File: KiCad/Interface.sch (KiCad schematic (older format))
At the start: 22 parts, among them J301 IR LED, J302 Button, SW301 Reset, SW302 Push 1, SW303 Push 2, U301 ULN2003

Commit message: Schematic Version 4 Some Software Changes
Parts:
- removed D301: LRTBG6TG, ledbox-newfootprints:LED-6-BIG, symbol LRTBG6TG
- removed R304: 150, Resistors_SMD:R_0805, symbol R
- removed R305, R311: 82, Resistors_SMD:R_0805, symbol R
- removed R306, R307: 22, Resistors_SMD:R_0805, symbol R
- removed U301: ULN2003, Housings_SOIC:SOIC-16_3.9x9.9mm_Pitch1.27mm, symbol ULN2003
- added C? (x2): 10u, Capacitors_SMD:C_0805, symbol C
- added JP?: IR 24mA, SMD_Jumper:Jumper_SMD_02, symbol Jumper_NO_Small
- added JP?: IR 48mA, SMD_Jumper:Jumper_SMD_02, symbol Jumper_NO_Small
- added JP?: IR 12mA, SMD_Jumper:Jumper_SMD_02, symbol Jumper_NO_Small
- added Q?: NTR4003N, TO_SOT_Packages_SMD:SOT-23, symbol Q_NMOS_GSD
- added R?: 100, Resistors_SMD:R_0805, symbol R
- added R?: 300, Resistors_SMD:R_0805, symbol R
- added R?: 150, Resistors_SMD:R_0805, symbol R
- added R?: 75, Resistors_SMD:R_0805, symbol R
- added R?: 100k, Resistors_SMD:R_0805, symbol R
- added TP?: IR PWM, symbol Test_Point
- added TP?: RGB Data 1, symbol Test_Point
- added TP?: RGB Data 2, symbol Test_Point
- added TP?: RGB Data 3, symbol Test_Point
- added TP?: IR LED, symbol Test_Point
- added U? (x3): WS2812B, LEDs:LED_WS2812B-PLCC4, symbol WS2812B
- D302, D303: footprint LEDs:LED_0805 -> LEDs:LED_D3.0mm
- SW301, SW302, SW303: Assembly (none) -> DNP
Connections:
- net +5V: now also C?.1, C?.1, U?.1 (VDD), U?.1 (VDD), U?.1 (VDD)
- net GND: now also C?.2, C?.2, Q?.2 (S), R?.1, U?.3 (GND), U?.3 (GND), U?.3 (GND)
- net IR_LED_DRV: now also R?.2, R?.2, R?.2, TP?.1
- net LED_IR: now also R?.2
- new net: Q?.1 (G), R?.1, R?.2
- new net: JP?.2, JP?.2, JP?.2, Q?.3 (D), TP?.1
- new net: JP?.1, R?.1 (x3)
- new net: TP?.1, U?.2 (DOUT), U?.4 (DIN) (x2)
- new net RGB_D: TP?.1, U?.4 (DIN)
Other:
- moved on the sheet: C301, C302, D302, D303, J301, J302, R301, R302, R303, R308, R309, R310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

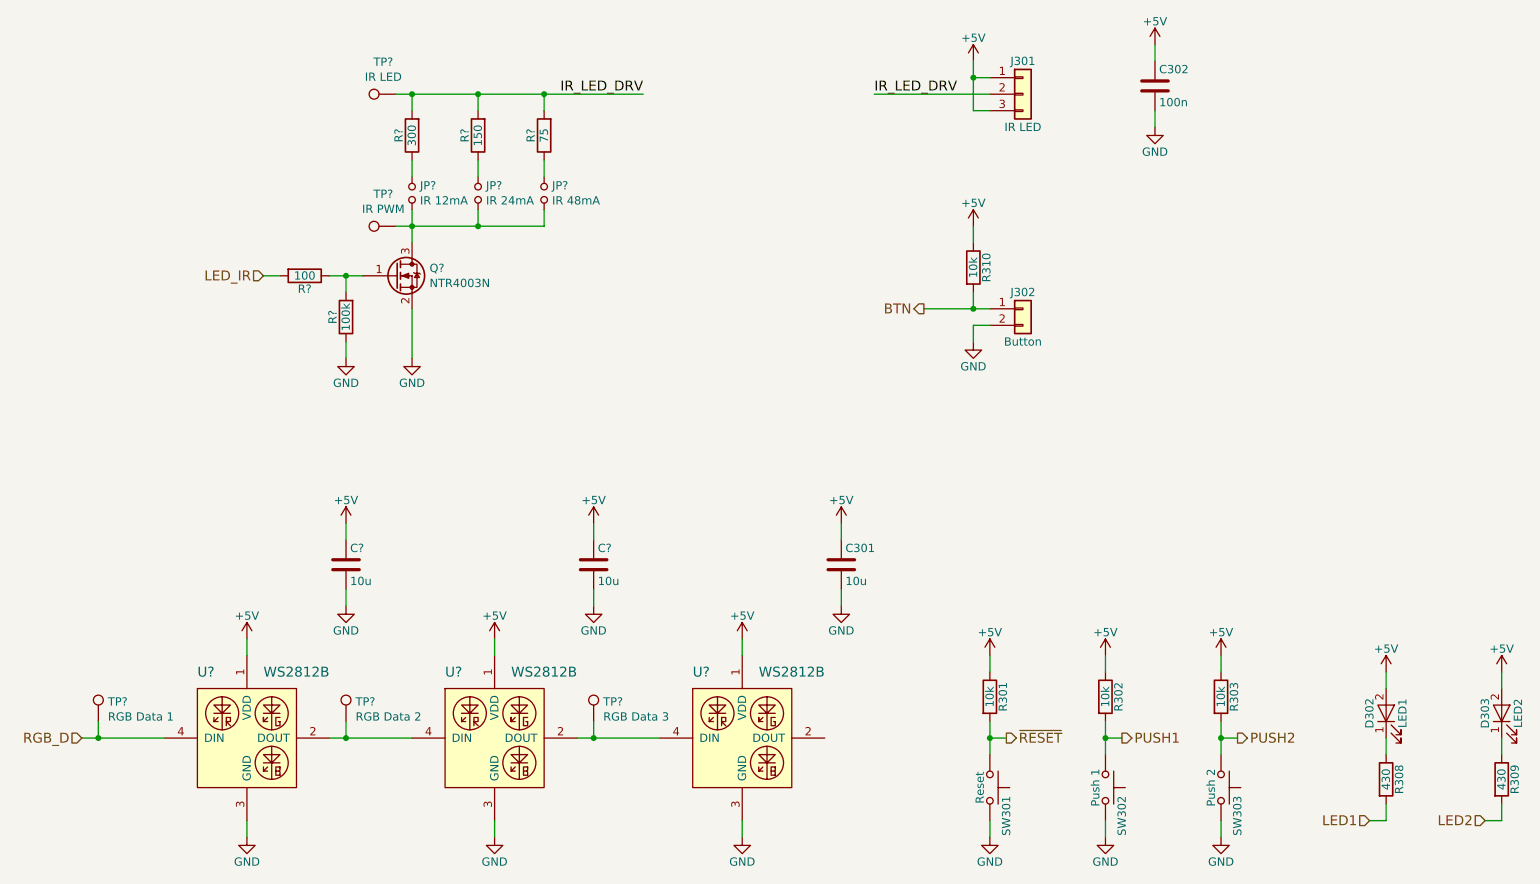
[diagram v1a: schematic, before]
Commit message: Changes to V4 Schematic, new Board design
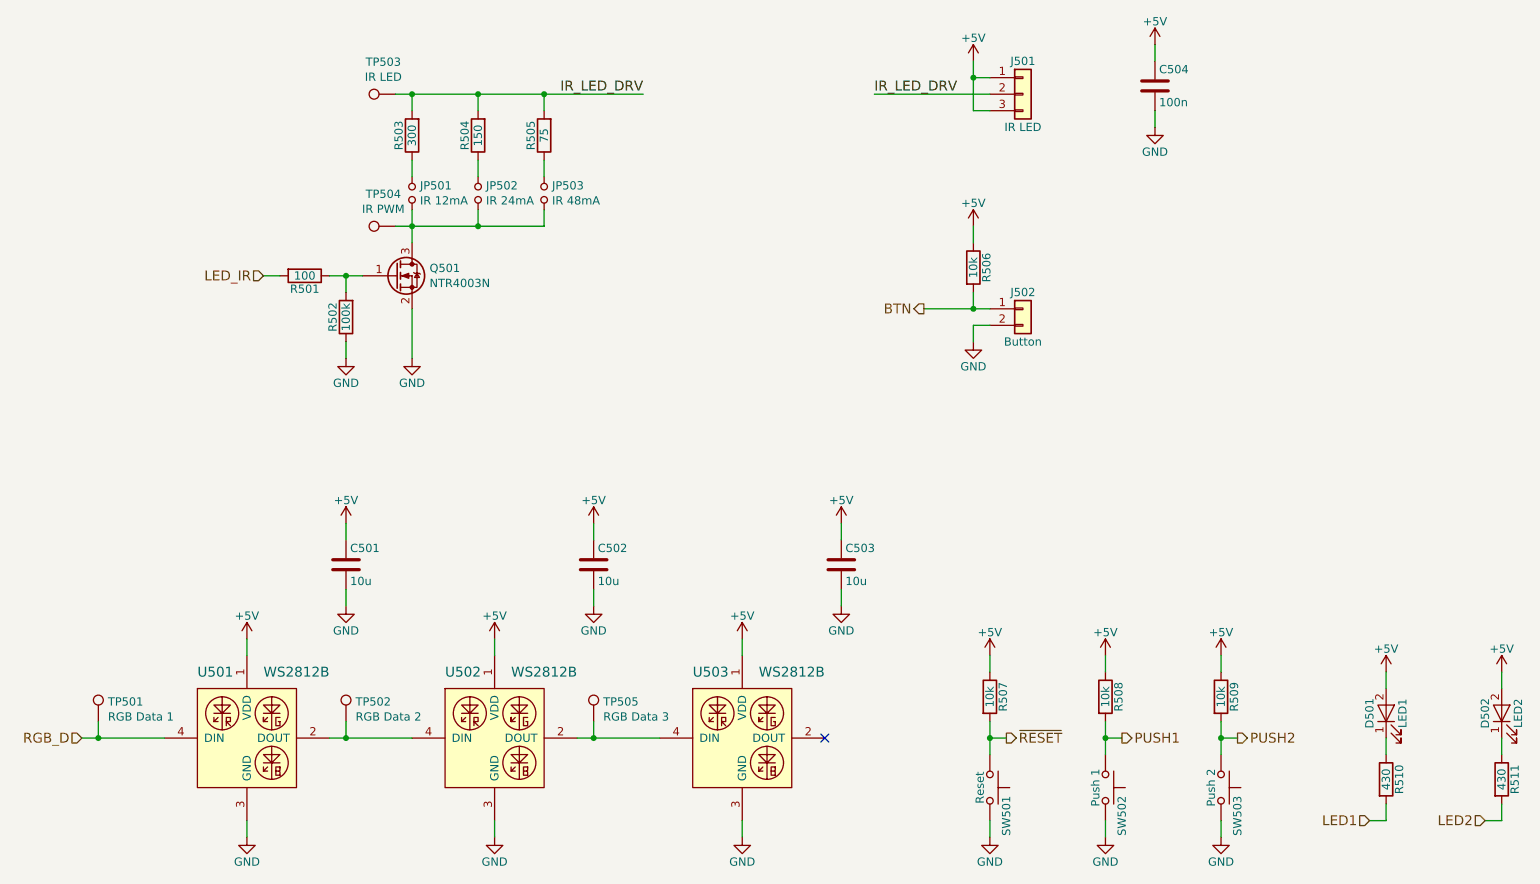
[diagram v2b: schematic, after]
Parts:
- J501: renamed from J301; footprint Pin_Headers:Pin_Header_Straight_1x03 -> Connectors_Molex:Molex_KK-6410-03_03x2.54mm_Straight
- J502: renamed from J302; footprint Pin_Headers:Pin_Header_Straight_1x02 -> Connectors_Molex:Molex_KK-6410-02_02x2.54mm_Straight
- TP501, TP502, TP503, TP504, TP505: renamed from TP?; footprint (none) -> Test:TEST_10
- gave numbers to parts that had none: 14
- renumbered C301 to C503, C302 to C504, D302 to D501, D303 to D502, R310 to R506, R301 to R507, R302 to R508, R303 to R509, R308 to R510, R309 to R511, SW301 to SW501, SW302 to SW502, SW303 to SW503
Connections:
- no-connect marks 0 -> 1

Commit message: Finished v4 board
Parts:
- TP501: value RGB Data 1 -> RGB1
- TP502: value RGB Data 2 -> RGB2
- TP505: value RGB Data 3 -> RGB3
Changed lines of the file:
@@
 P 1800 5200
 F 0 "TP501" H 1858 5320 50  0000 L CNN
-F 1 "RGB Data 1" H 1858 5229 50  0000 L CNN
+F 1 "RGB1" H 1858 5229 50  0000 L CNN
 F 2 "Test:TEST_10" H 2000 5200 50  0001 C CNN
 F 3 "~" H 2000 5200 50  0001 C CNN
@@
 P 3300 5200
 F 0 "TP502" H 3358 5320 50  0000 L CNN
-F 1 "RGB Data 2" H 3358 5229 50  0000 L CNN
+F 1 "RGB2" H 3358 5229 50  0000 L CNN
 F 2 "Test:TEST_10" H 3500 5200 50  0001 C CNN
 F 3 "~" H 3500 5200 50  0001 C CNN
@@
 P 4800 5200
 F 0 "TP505" H 4858 5320 50  0000 L CNN
-F 1 "RGB Data 3" H 4858 5229 50  0000 L CNN
+F 1 "RGB3" H 4858 5229 50  0000 L CNN
 F 2 "Test:TEST_10" H 5000 5200 50  0001 C CNN
 F 3 "~" H 5000 5200 50  0001 C CNN
